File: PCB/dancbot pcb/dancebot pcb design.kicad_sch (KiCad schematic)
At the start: 28 parts, among them J1 ESP32-PICO-KIT-V4.1, J2 Voltage Regulator, J3 Board Pins, J4 Pins, J6 Conn_01x04_Socket, J7 Conn_01x04_Socket, Q1 IRLML6402TRPBF, Q2 IRLML2502, Q3 2N3904, Q4 PMOS, SW1 SP switch, SW2 SW_SPST

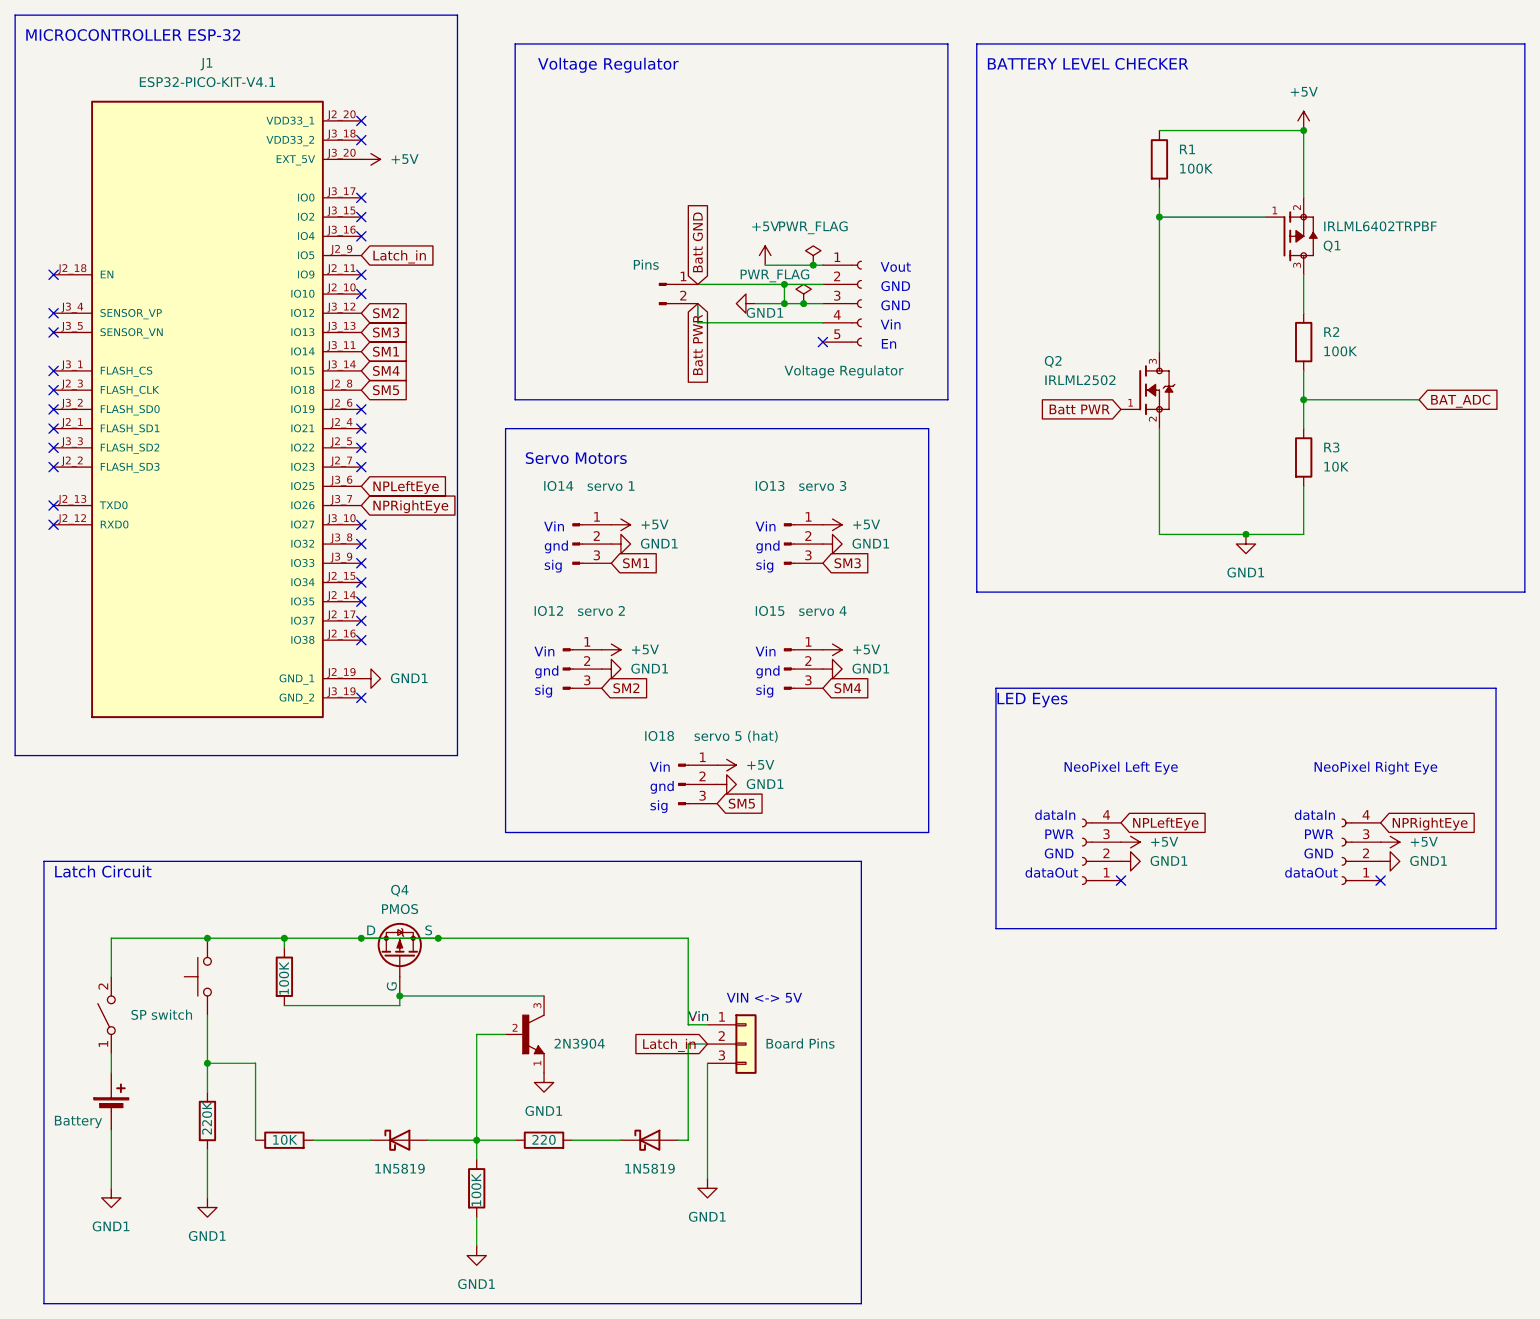
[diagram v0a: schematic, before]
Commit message: Correct Schematic File
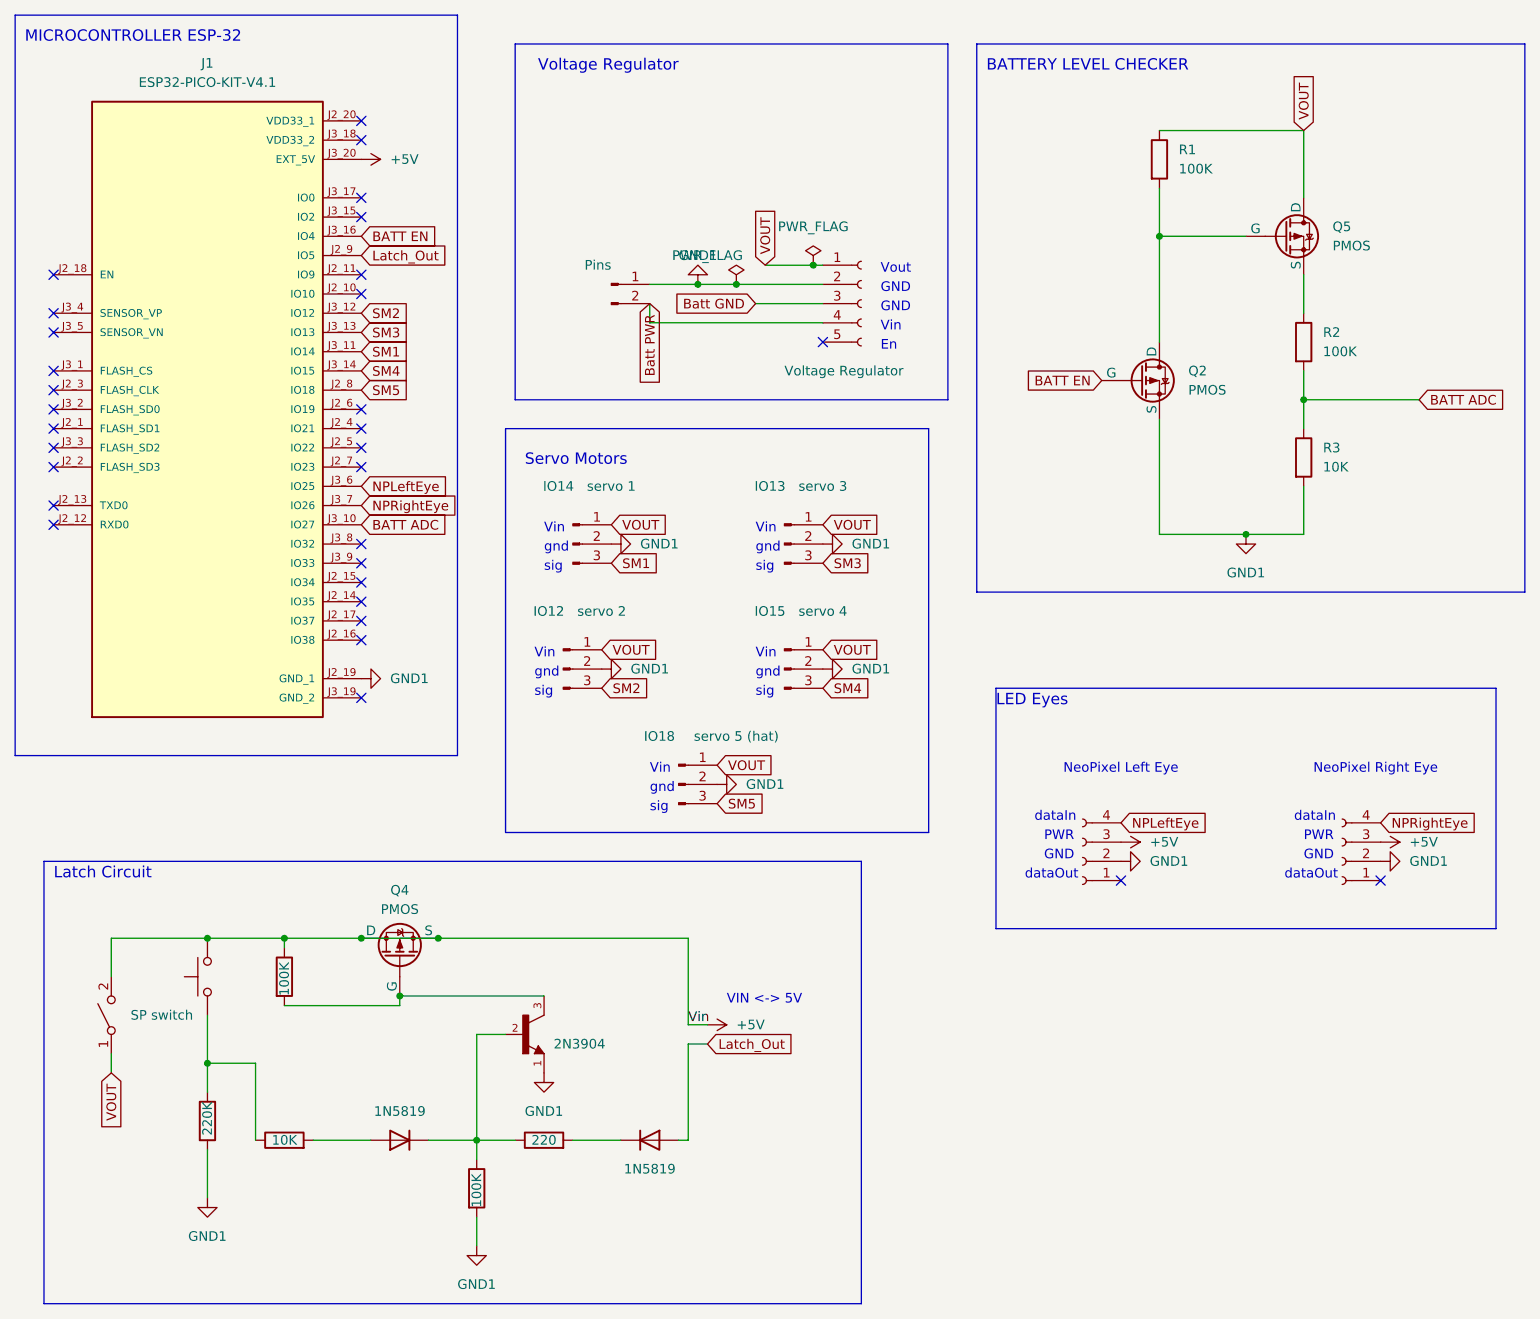
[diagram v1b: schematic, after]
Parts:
- removed BT1: Battery, symbol Device:Battery_Cell
- removed J3: Board Pins, symbol Connector_Generic:Conn_01x03
- removed Q1: IRLML6402TRPBF, IRLML6402TRPBF:SOT95P237X112-3N, symbol IRLML6402TRPBF:IRLML6402TRPBF
- removed Q2: IRLML2502, IRLML2502:SOT95P237X112-3N, symbol IRLML2502:IRLML2502
- added Q2, Q5: PMOS, dancebot pcb libraries stuff:TO254P1052X465X1989-3, symbol Simulation_SPICE:PMOS
- D1, D2: symbol Diode:1N5819 -> Diode:1N4006
- J4: footprint (none) -> Connector_PinHeader_1.00mm:PinHeader_1x02_P1.00mm_Vertical
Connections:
- net BAT_ADC is gone; now on net BATT ADC: R2.2, R3.1
- net Vin is gone; now on net +5V: Q4.1 (D), Q4.3 (S), R5.1, SW1.2, SW2.2 (B)
- net +5V: no longer IO12.1 (Pin_1), IO13.1 (Pin_1), IO14.1 (Pin_1), IO15.1 (Pin_1), IO18.1 (Pin_1), J2.1 (Pin_1), R1.1
- net GND1: now also Q2.3 (S); no longer J2.3 (Pin_3)
- net at R6.2: now also D1.2 (A); no longer D1.1 (K)
- net VOUT: now reaches SW2.1 (A)
- net VOUT: now also IO12.1 (Pin_1), IO13.1 (Pin_1), IO14.1 (Pin_1), IO15.1 (Pin_1), IO18.1 (Pin_1), J2.1 (Pin_1), R1.1, Q5.1 (D)
- net at R1.2: now also Q2.1 (D), Q5.2 (G)
- net at R2.1: now also Q5.3 (S)
- net BATT ADC: now reaches J1.J3_10 (IO27)
- net BATT EN: now reaches J1.J3_16 (IO4)
- net BATT EN: now also Q2.2 (G)
- net at Q3.2, R7.1, R8.1: now also D1.1 (K); no longer D1.2 (A)
- net Latch_in renamed Latch_Out
- new net Batt GND: J2.3 (Pin_3)
- no-connect marks 33 -> 31

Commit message: Connections For Layout Revision 2
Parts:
- removed Q4: PMOS, dancebot pcb libraries stuff:TO254P1052X465X1989-3, symbol Simulation_SPICE:PMOS
- added Q1: PMOS, dancebot pcb libraries stuff:TO254P1052X465X1989-3, symbol Simulation_SPICE:PMOS
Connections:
- net +5V: now also Q1.3 (S); no longer R5.1, SW1.2, SW2.2 (B)
- net at Q3.3, R5.2: now also Q1.2 (G)
- new net: Q1.1 (D), R5.1, SW1.2, SW2.2 (B)
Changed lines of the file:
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@@
 (kicad_sch (version 20230121) (generator eeschema)
   (paper "A4")
-  (junction (at 72.39 137.16) (diameter 0) (color 0 0 0 0)
-  )
   (junction (at 111.76 50.8) (diameter 0) (color 0 0 0 0)
   )
@@
   )
   (junction (at 77.47 163.83) (diameter 0) (color 0 0 0 0)
-  )
-  (junction (at 62.23 137.16) (diameter 0) (color 0 0 0 0)
   )
   (junction (at 121.92 48.26) (diameter 0) (color 0 0 0 0)
@@
     (stroke (width 0) (type default))
   )
-  (wire (pts (xy 62.23 137.16) (xy 72.39 137.16))
-    (stroke (width 0) (type default))
-  )
   (wire (pts (xy 41.91 153.67) (xy 48.26 153.67))
     (stroke (width 0) (type default))
@@
         (path "/a5572283-9a9d-4246-8741-667ff8a68ceb"
           (reference "R5") (unit 1)
+        )
+      )
+    )
+  )
+  (symbol (lib_id "Simulation_SPICE:PMOS") (at 67.31 139.7 90) (unit 1)
+    (in_bom yes) (on_board yes) (dnp no) (fields_autoplaced)
+    (property "Reference" "Q1" (at 67.31 130.81 90)
+      (effects (font (size 1.27 1.27)))
+    )
+    (property "Value" "PMOS" (at 67.31 133.35 90)
+      (effects (font (size 1.27 1.27)))
+    )
+    (property "Footprint" "dancebot pcb libraries stuff:TO254P1052X465X1989-3" (at 64.77 134.62 0)
+      (effects (font (size 1.27 1.27)) hide)
+    )
+    (property "Datasheet" "https://ngspice.sourceforge.io/docs/ngspice-manual.pdf" (at 80.01 139.7 0)
+      (effects (font (size 1.27 1.27)) hide)
+    )
+    (property "Sim.Device" "PMOS" (at 84.455 139.7 0)
+      (effects (font (size 1.27 1.27)) hide)
+    )
+    (property "Sim.Type" "VDMOS" (at 86.36 139.7 0)
+      (effects (font (size 1.27 1.27)) hide)
+    )
+    (property "Sim.Pins" "1=D 2=G 3=S" (at 82.55 139.7 0)
+      (effects (font (size 1.27 1.27)) hide)
+    )
+    (pin "1")
+    (pin "2")
+    (pin "3")
+    (instances
+      (project "dancebot pcb design"
+        (path "/a5572283-9a9d-4246-8741-667ff8a68ceb"
+          (reference "Q1") (unit 1)
         )
       )
@@
         )
       )
-    )
-  )
-  (symbol (lib_id "Simulation_SPICE:PMOS") (at 67.31 139.7 90) (unit 1)
-    (in_bom yes) (on_board yes) (dnp no) (fields_autoplaced)
-    (property "Reference" "Q4" (at 67.31 130.81 90)
-      (effects (font (size 1.27 1.27)))
-    )
-    (property "Value" "PMOS" (at 67.31 133.35 90)
-      (effects (font (size 1.27 1.27)))
-    )
-    (property "Footprint" "dancebot pcb libraries stuff:TO254P1052X465X1989-3" (at 64.77 134.62 0)
-      (effects (font (size 1.27 1.27)) hide)
-    )
-    (property "Datasheet" "https://ngspice.sourceforge.io/docs/ngspice-manual.pdf" (at 80.01 139.7 0)
-      (effects (font (size 1.27 1.27)) hide)
-    )
-    (property "Sim.Device" "PMOS" (at 84.455 139.7 0)
-      (effects (font (size 1.27 1.27)) hide)
-    )
-    (property "Sim.Type" "VDMOS" (at 86.36 139.7 0)
-      (effects (font (size 1.27 1.27)) hide)
-    )
-    (property "Sim.Pins" "1=D 2=G 3=S" (at 82.55 139.7 0)
-      (effects (font (size 1.27 1.27)) hide)
-    )
-    (pin "1")
-    (pin "2")
-    (pin "3")
-    (instances
-      (project "dancebot pcb design"
-        (path "/a5572283-9a9d-4246-8741-667ff8a68ceb"
-          (reference "Q4") (unit 1)
-        )
-      )
